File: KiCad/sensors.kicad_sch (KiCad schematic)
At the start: 8 parts, among them U6 LTR-303ALS-01

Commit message: Added sheet notes and initial design template, reordered microcontoller subsheet and add microntoller subsheet notes
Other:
- company: (none) -> UCT
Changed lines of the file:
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@@
 (kicad_sch (version 20230121) (generator eeschema)
   (paper "A4")
+  (title_block
+    (date "2023-03-11")
+    (company "UCT")
+  )
   (junction (at 190.5 41.91) (diameter 0) (color 0 0 0 0)
   )

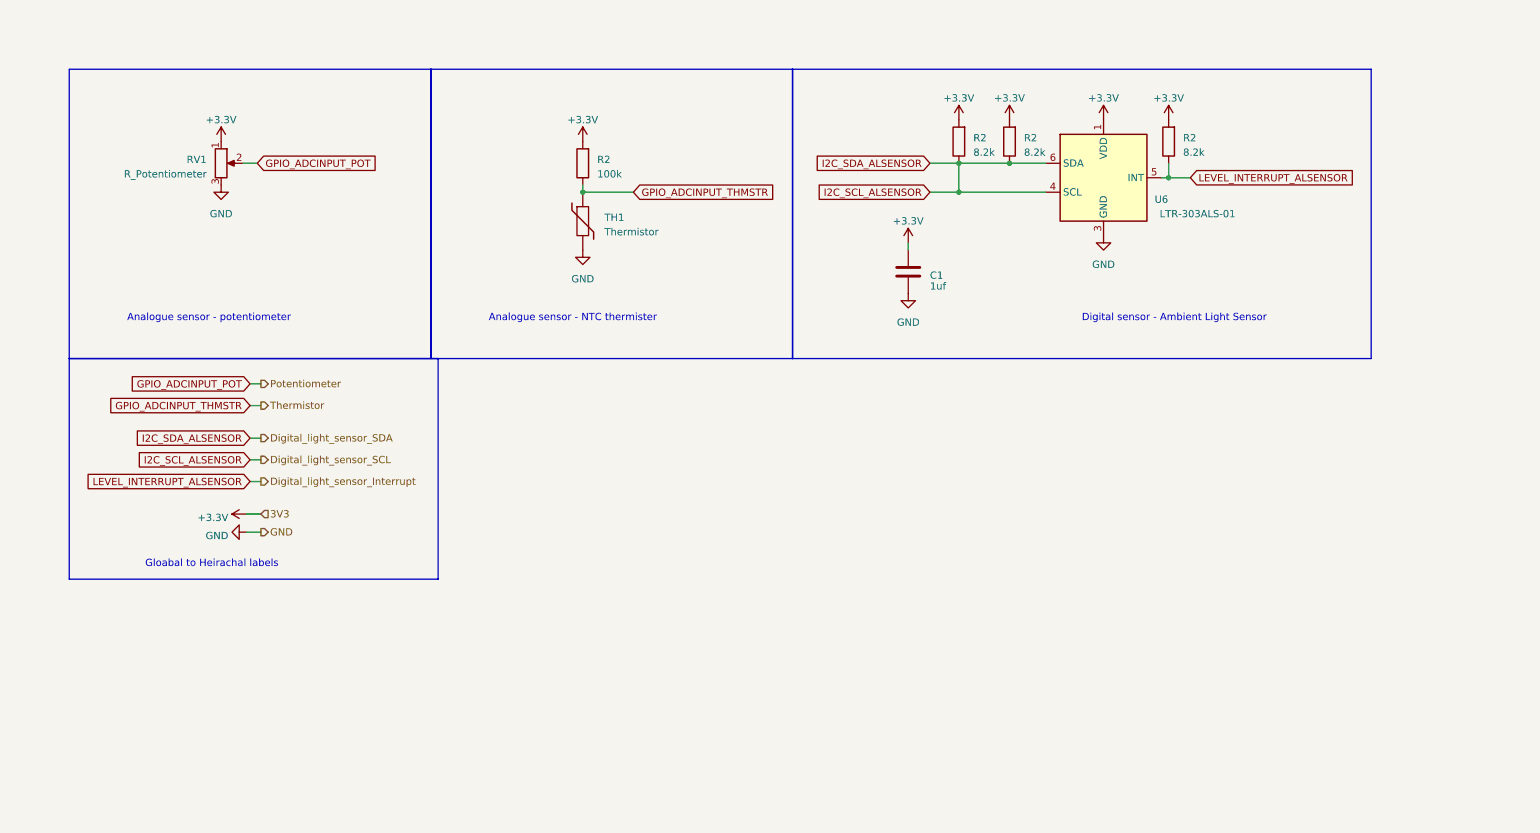
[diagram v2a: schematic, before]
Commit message: started adding temperature & humidity sensor to sensors schematic, small changes to rob week 4 doc
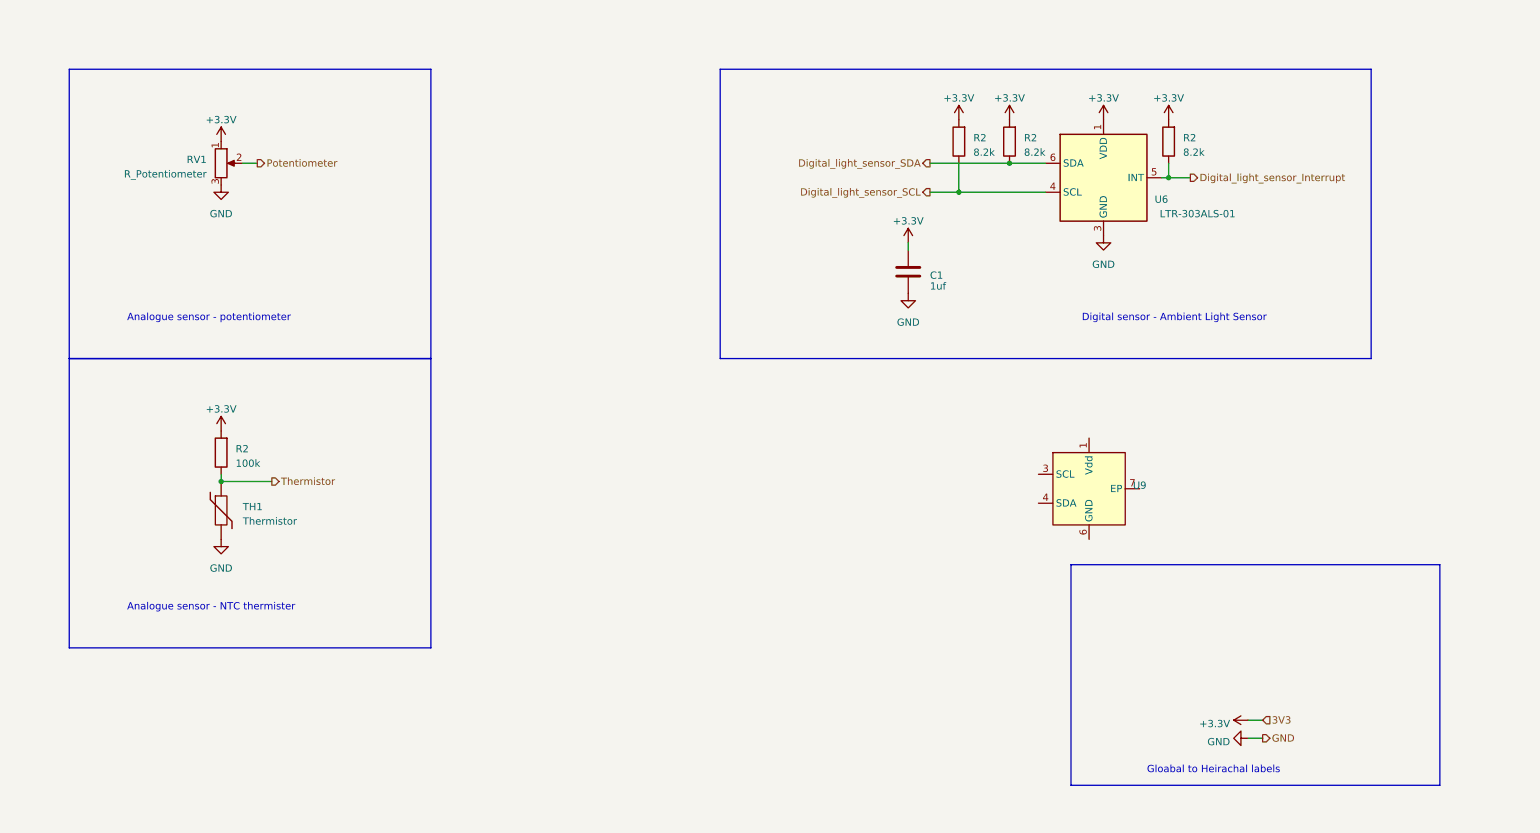
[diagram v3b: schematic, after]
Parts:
- added U9: ~, symbol sensor_components_library:GXHTC3
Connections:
- net GPIO_ADCINPUT_POT renamed Potentiometer
- net GPIO_ADCINPUT_THMSTR renamed Thermistor
- net I2C_SCL_ALSENSOR renamed Digital_light_sensor_SCL
- net Digital_light_sensor_SCL: no longer R2.1, U6.6 (SDA)
- net LEVEL_INTERRUPT_ALSENSOR renamed Digital_light_sensor_Interrupt
- new net Digital_light_sensor_SDA: R2.1, U6.6 (SDA)
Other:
- moved on the sheet: R2, TH1

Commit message: changes to sensor schematic :
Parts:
- removed R2 (x3): 8.2k, symbol Device:R
- removed U9: ~, symbol sensor_components_library:GXHTC3
- added C1: 100n, symbol Device:C
- added R11 (x10): 0, symbol Device:R
- added U8: GXHTC3, symbol sensor_components_library:GXHTC3
- C1: value 1uf -> 1u
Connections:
- net +3.3V: now also C1.1, R11.2, R11.2, R11.2, R11.2; no longer R2.2, RV1.1, U6.1 (VDD)
- net GND: now also C1.2, U8.6 (GND)
- net Potentiometer: now also R11.1; no longer RV1.2
- net Thermistor: now also R11.1; no longer R2.1, TH1.1
- net Digital_light_sensor_SCL: no longer names the net of U6.4 (SCL)
- net Digital_light_sensor_SCL: now also R11.2
- net Digital_light_sensor_SDA: no longer names the net of U6.6 (SDA)
- net Digital_light_sensor_SDA: now also R11.1
- new net: R11.1, U8.3 (SCL)
- new net: R11.2, R2.1, TH1.1
- new net: R11.1, R2.2
- new net: R11.1, RV1.1
- new net: R11.2, RV1.2
- new net: R11.1, U6.1 (VDD)
- new net: R11.1, U8.1 (VDD)
- new net: R11.1, U8.4 (SDA)
- new net Sensors_SCL: R11.1, R11.2
- new net Sensors_SDA: R11.2, R11.2
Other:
- note added: "Digital sensor - Temperature/Humidity Sensor"
- note added: "I2C and interrupt pullup resistors on microcontroller schematic"
- note added: "I2C hierachical label attachments"
- note added: "I2C pullup resistors on microcontroller schematic"
- note removed: "Gloabal to Heirachal labels"
- title: (none) -> Sensors Subsystem Schematic
- moved on the sheet: C1, R2, RV1, TH1, U6

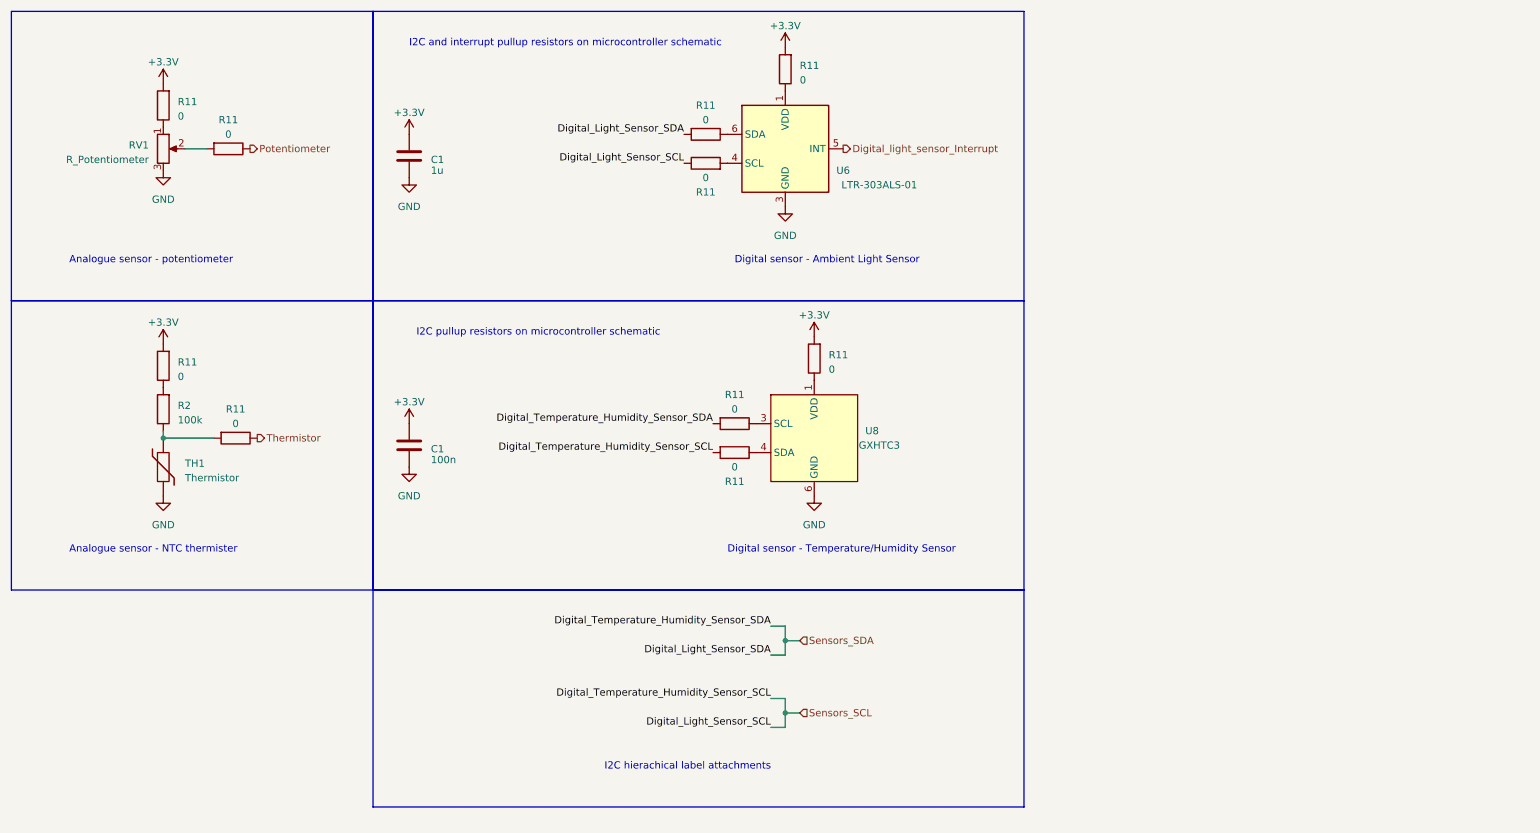
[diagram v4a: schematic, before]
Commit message: updated sensor and microcontroller schematics
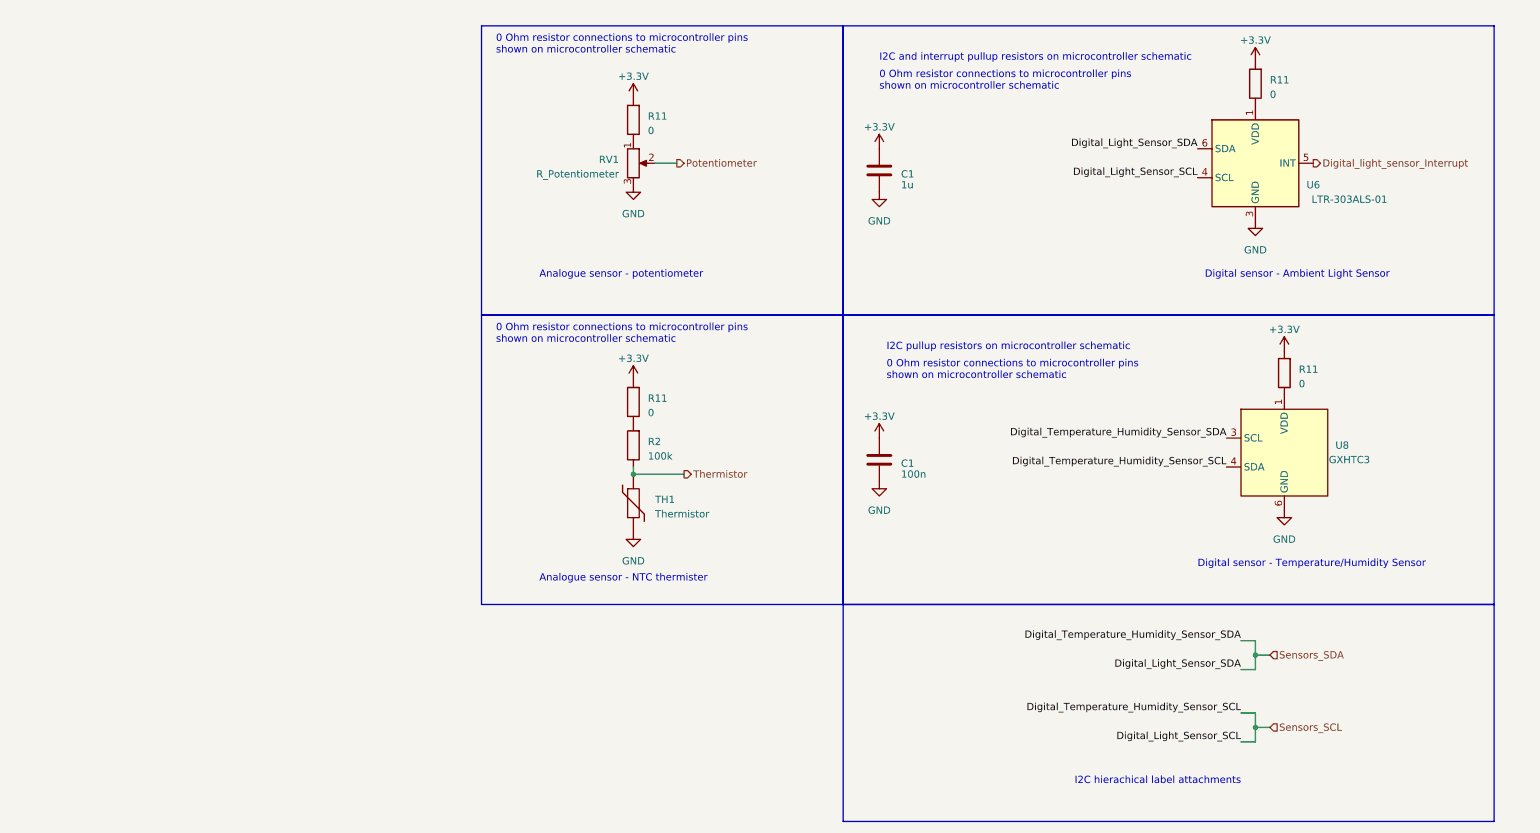
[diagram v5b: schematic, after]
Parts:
- removed R11 (x6): 0, symbol Device:R
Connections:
- net Potentiometer: now also RV1.2
- net Sensors_SCL: now also U6.4 (SCL), U8.4 (SDA)
- net Sensors_SDA: now also U6.6 (SDA), U8.3 (SCL)
- net Thermistor: now also R2.1, TH1.1
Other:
- note added: "0 Ohm resistor connections to microcontroller pins shown on microcontroller schematic"
- moved on the sheet: C1, R11, R2, RV1, TH1, U6, U8

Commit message: git commit
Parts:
- R2: JLC code (none) -> C17900; Part name (none) -> 1206W4F1003T5E
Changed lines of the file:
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@@
+      (effects (font (size 1.27 1.27)) hide)
+    )
+    (property "DNF" "" (at 124.46 91.44 0)
+      (effects (font (size 1.27 1.27)) hide)
+    )
+    (property "Extended Part Cost" "" (at 124.46 91.44 0)
+      (effects (font (size 1.27 1.27)) hide)
+    )
+    (property "JLC code" "C17900" (at 124.46 91.44 0)
+      (effects (font (size 1.27 1.27)) hide)
+    )
+    (property "Part name" "1206W4F1003T5E" (at 124.46 91.44 0)
+      (effects (font (size 1.27 1.27)) hide)
+    )
+    (property "cost per unit" "" (at 124.46 91.44 0)
       (effects (font (size 1.27 1.27)) hide)
     )
@@
       (effects (font (size 1.27 1.27)) hide)
     )
+    (property "DNF" "" (at 167.64 43.18 0)
+      (effects (font (size 1.27 1.27)) hide)
+    )
+    (property "Extended Part Cost" "" (at 167.64 43.18 0)
+      (effects (font (size 1.27 1.27)) hide)
+    )
+    (property "JLC code" "" (at 167.64 43.18 0)
+      (effects (font (size 1.27 1.27)) hide)
+    )
+    (property "Part name" "" (at 167.64 43.18 0)
+      (effects (font (size 1.27 1.27)) hide)
+    )
+    (property "cost per unit" "" (at 167.64 43.18 0)
+      (effects (font (size 1.27 1.27)) hide)
+    )
     (pin "1")
     (pin "2")
@@
     )
     (property "Datasheet" "~" (at 124.46 41.91 0)
+      (effects (font (size 1.27 1.27)) hide)
+    )
+    (property "DNF" "" (at 124.46 41.91 0)
+      (effects (font (size 1.27 1.27)) hide)
+    )
+    (property "Extended Part Cost" "" (at 124.46 41.91 0)
+      (effects (font (size 1.27 1.27)) hide)
+    )
+    (property "JLC code" "" (at 124.46 41.91 0)
+      (effects (font (size 1.27 1.27)) hide)
+    )
+    (property "Part name" "" (at 124.46 41.91 0)
+      (effects (font (size 1.27 1.27)) hide)
+    )
+    (property "cost per unit" "" (at 124.46 41.91 0)
       (effects (font (size 1.27 1.27)) hide)
     )
@@
       (effects (font (size 1.27 1.27)) hide)
     )
+    (property "DNF" "" (at 167.64 93.98 0)
+      (effects (font (size 1.27 1.27)) hide)
+    )
+    (property "Extended Part Cost" "" (at 167.64 93.98 0)
+      (effects (font (size 1.27 1.27)) hide)
+    )
+    (property "JLC code" "" (at 167.64 93.98 0)
+      (effects (font (size 1.27 1.27)) hide)
+    )
+    (property "Part name" "" (at 167.64 93.98 0)
+      (effects (font (size 1.27 1.27)) hide)
+    )
+    (property "cost per unit" "" (at 167.64 93.98 0)
+      (effects (font (size 1.27 1.27)) hide)
+    )
     (pin "1")
     (pin "2")
@@
     )
     (property "Datasheet" "http://optoelectronics.liteon.com/upload/download/DS86-2013-0004/LTR-303ALS-01_DS_V1.pdf" (at 226.06 33.02 0)
+      (effects (font (size 1.27 1.27)) hide)
+    )
+    (property "DNF" "" (at 233.68 41.91 0)
+      (effects (font (size 1.27 1.27)) hide)
+    )
+    (property "Extended Part Cost" "" (at 233.68 41.91 0)
+      (effects (font (size 1.27 1.27)) hide)
+    )
+    (property "JLC code" "" (at 233.68 41.91 0)
+      (effects (font (size 1.27 1.27)) hide)
+    )
+    (property "Part name" "" (at 233.68 41.91 0)
+      (effects (font (size 1.27 1.27)) hide)
+    )
+    (property "cost per unit" "" (at 233.68 41.91 0)
       (effects (font (size 1.27 1.27)) hide)
     )
@@
       (effects (font (size 1.27 1.27)) hide)
     )
+    (property "DNF" "" (at 124.46 34.29 0)
+      (effects (font (size 1.27 1.27)) hide)
+    )
+    (property "Extended Part Cost" "" (at 124.46 34.29 0)
+      (effects (font (size 1.27 1.27)) hide)
+    )
+    (property "JLC code" "" (at 124.46 34.29 0)
+      (effects (font (size 1.27 1.27)) hide)
+    )
+    (property "Part name" "" (at 124.46 34.29 0)
+      (effects (font (size 1.27 1.27)) hide)
+    )
+    (property "cost per unit" "" (at 124.46 34.29 0)
+      (effects (font (size 1.27 1.27)) hide)
+    )
     (pin "1")
     (pin "2")
@@
     )
     (property "Datasheet" "~" (at 238.76 78.74 0)
+      (effects (font (size 1.27 1.27)) hide)
+    )
+    (property "DNF" "" (at 238.76 78.74 0)
+      (effects (font (size 1.27 1.27)) hide)
+    )
+    (property "Extended Part Cost" "" (at 238.76 78.74 0)
+      (effects (font (size 1.27 1.27)) hide)
+    )
+    (property "JLC code" "" (at 238.76 78.74 0)
+      (effects (font (size 1.27 1.27)) hide)
+    )
+    (property "Part name" "" (at 238.76 78.74 0)
+      (effects (font (size 1.27 1.27)) hide)
+    )
+    (property "cost per unit" "" (at 238.76 78.74 0)
       (effects (font (size 1.27 1.27)) hide)
     )
@@
       (effects (font (size 1.27 1.27)) hide)
     )
+    (property "DNF" "" (at 238.76 92.71 0)
+      (effects (font (size 1.27 1.27)) hide)
+    )
+    (property "Extended Part Cost" "" (at 238.76 92.71 0)
+      (effects (font (size 1.27 1.27)) hide)
+    )
+    (property "JLC code" "" (at 238.76 92.71 0)
+      (effects (font (size 1.27 1.27)) hide)
+    )
+    (property "Part name" "" (at 238.76 92.71 0)
+      (effects (font (size 1.27 1.27)) hide)
+    )
+    (property "cost per unit" "" (at 238.76 92.71 0)
+      (effects (font (size 1.27 1.27)) hide)
+    )
     (pin "1")
     (pin "3")
@@
       (effects (font (size 1.27 1.27)) hide)
     )
+    (property "DNF" "" (at 233.68 27.94 0)
+      (effects (font (size 1.27 1.27)) hide)
+    )
+    (property "Extended Part Cost" "" (at 233.68 27.94 0)
+      (effects (font (size 1.27 1.27)) hide)
+    )
+    (property "JLC code" "" (at 233.68 27.94 0)
+      (effects (font (size 1.27 1.27)) hide)
+    )
+    (property "Part name" "" (at 233.68 27.94 0)
+      (effects (font (size 1.27 1.27)) hide)
+    )
+    (property "cost per unit" "" (at 233.68 27.94 0)
+      (effects (font (size 1.27 1.27)) hide)
+    )
     (pin "1")
     (pin "2")
@@
       (effects (font (size 1.27 1.27)) hide)
     )
+    (property "DNF" "" (at 124.46 83.82 0)
+      (effects (font (size 1.27 1.27)) hide)
+    )
+    (property "Extended Part Cost" "" (at 124.46 83.82 0)
+      (effects (font (size 1.27 1.27)) hide)
+    )
+    (property "JLC code" "" (at 124.46 83.82 0)
+      (effects (font (size 1.27 1.27)) hide)
+    )
+    (property "Part name" "" (at 124.46 83.82 0)
+      (effects (font (size 1.27 1.27)) hide)
+    )
+    (property "cost per unit" "" (at 124.46 83.82 0)
+      (effects (font (size 1.27 1.27)) hide)
+    )
     (pin "1")
     (pin "2")
@@
       (effects (font (size 1.27 1.27)) hide)
     )
+    (property "DNF" "" (at 124.46 101.6 0)
+      (effects (font (size 1.27 1.27)) hide)
+    )
+    (property "Extended Part Cost" "" (at 124.46 101.6 0)
+      (effects (font (size 1.27 1.27)) hide)
+    )
+    (property "JLC code" "" (at 124.46 101.6 0)
+      (effects (font (size 1.27 1.27)) hide)
+    )
+    (property "Part name" "" (at 124.46 101.6 0)
+      (effects (font (size 1.27 1.27)) hide)
+    )
+    (property "cost per unit" "" (at 124.46 101.6 0)
+      (effects (font (size 1.27 1.27)) hide)
+    )

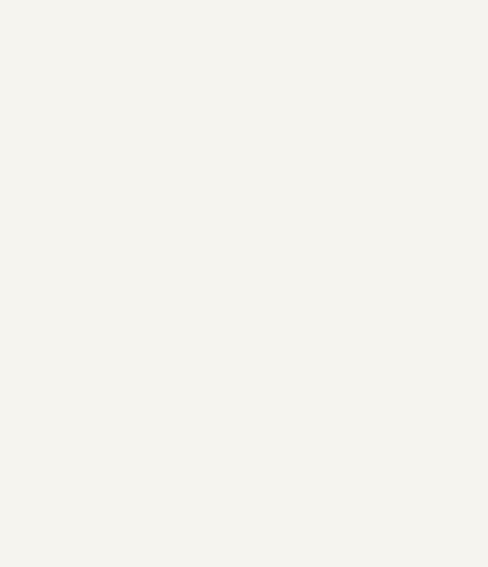
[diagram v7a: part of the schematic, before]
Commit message: added test point
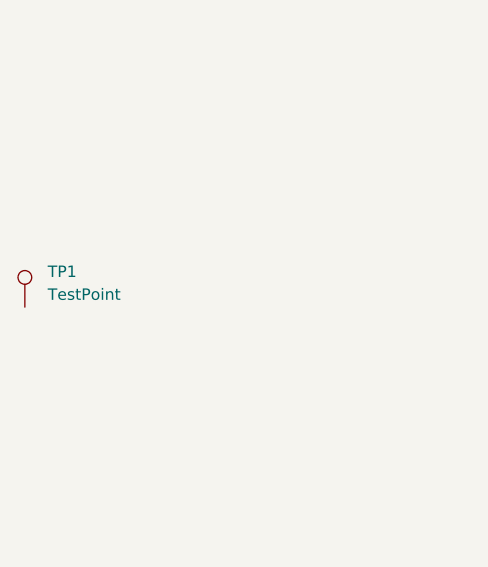
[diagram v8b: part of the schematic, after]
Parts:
- added TP1: TestPoint, symbol Connector:TestPoint
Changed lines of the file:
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@@
+    )
+  )
+  (symbol (lib_id "Connector:TestPoint") (at 36.83 72.39 0) (unit 1)
+    (in_bom yes) (on_board yes) (dnp no) (fields_autoplaced)
+    (property "Reference" "TP1" (at 39.37 68.453 0)
+      (effects (font (size 1.27 1.27)) (justify left))
+    )
+    (property "Value" "TestPoint" (at 39.37 70.993 0)
+      (effects (font (size 1.27 1.27)) (justify left))
+    )
+    (property "Footprint" "" (at 41.91 72.39 0)
+      (effects (font (size 1.27 1.27)) hide)
+    )
+    (property "Datasheet" "~" (at 41.91 72.39 0)
+      (effects (font (size 1.27 1.27)) hide)
+    )
+    (pin "1")
+    (instances
+      (project "EEE3088F_CKR"
+        (path "/31e5d740-f3fb-4029-be8d-dfdc4f653d72/fd4dbd89-ce5b-45e9-b49b-ec599df435f0"
+          (reference "TP1") (unit 1)
+        )
+      )
     )
   )
